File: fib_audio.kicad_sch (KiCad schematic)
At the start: 58 parts, among them J701 DNP AUDIO-JACK-8P-SMD, J702 SPK_JST_L, J703 SPK_JST_R, K701 BUTTON-4PDTSM-62K-S-V-T/R(SN4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, U701 WM8960CGEFL, X701 24MHz 306020014

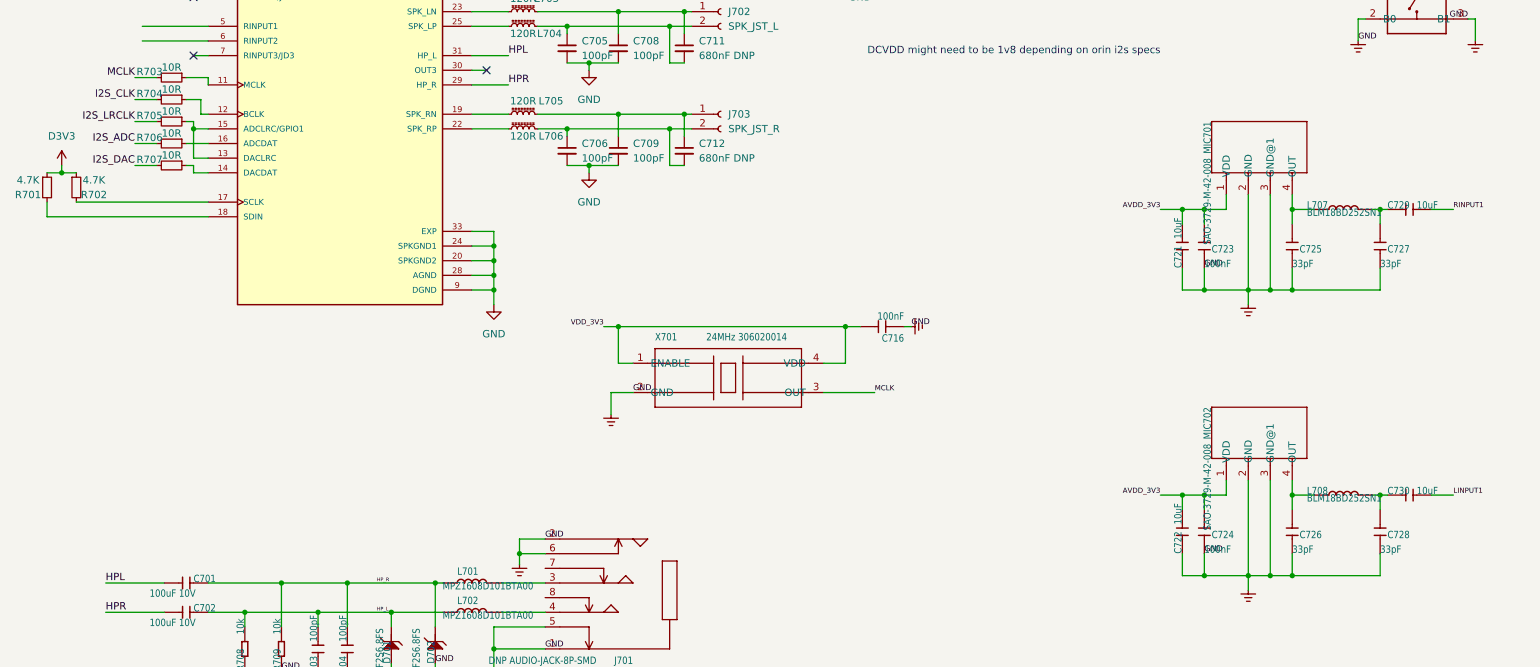
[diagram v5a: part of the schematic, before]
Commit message: added notest regarding the audio codec
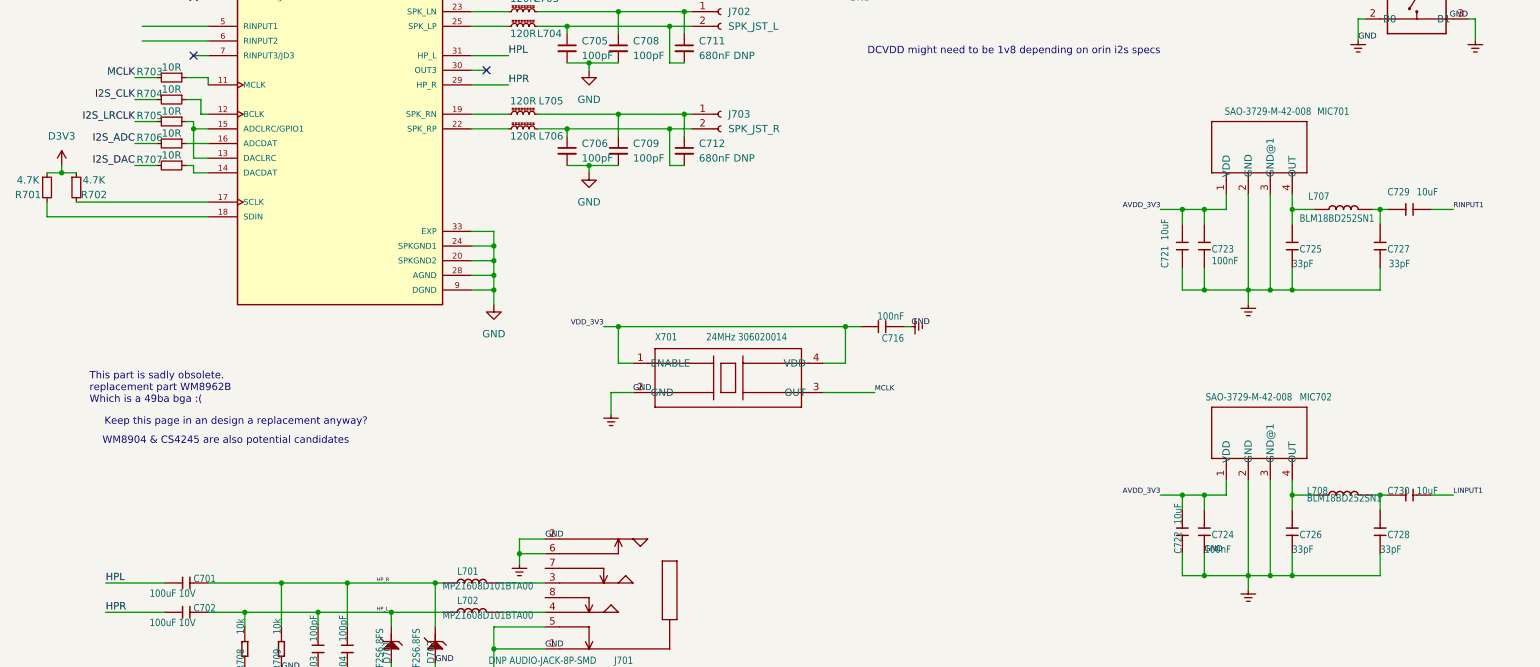
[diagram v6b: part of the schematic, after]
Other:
- note added: "Keep this page in an design a replacement anyway?"
- note added: "This part is sadly obsolete. replacement part WM8962B Which is a 49ba bga :("
- note added: "WM8904 & CS4245 are also potential candidates"
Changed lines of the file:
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@@
 	)
 	(junction
+		(at 222.25 95.25)
+		(diameter 0)
+		(color 0 0 0 0)
+	)
+	(junction
 		(at 140.97 36.83)
 		(diameter 0)
@@
 	)
 	(junction
-		(at 222.25 95.25)
-		(diameter 0)
-		(color 0 0 0 0)
-	)
-	(junction
 		(at 115.57 55.88)
 		(diameter 0)
@@
 	(wire
 		(pts
-			(xy 229.87 95.25) (xy 222.25 95.25)
-		)
-		(stroke
-			(width 0.1524)
-			(type solid)
-		)
-	)
-	(wire
-		(pts
 			(xy 132.08 46.99) (xy 133.35 46.99)
 		)
@@
 	(wire
 		(pts
+			(xy 222.25 95.25) (xy 229.87 95.25)
+		)
+		(stroke
+			(width 0)
+			(type default)
+		)
+	)
+	(wire
+		(pts
 			(xy 119.38 113.03) (xy 119.38 116.84)
 		)
@@
 	(wire
 		(pts
+			(xy 222.25 95.25) (xy 222.25 91.44)
+		)
+		(stroke
+			(width 0)
+			(type default)
+		)
+	)
+	(wire
+		(pts
 			(xy 130.81 31.75) (xy 130.81 36.83)
 		)
@@
 	(wire
 		(pts
-			(xy 222.25 91.44) (xy 222.25 95.25)
-		)
-		(stroke
-			(width 0.1524)
-			(type solid)
-		)
-	)
-	(wire
-		(pts
 			(xy 36.83 69.85) (xy 40.64 69.85)
 		)
@@
 		)
 	)
+	(text "WM8904 & CS4245 are also potential candidates"
+		(exclude_from_sim no)
+		(at 52.578 121.412 0)
+		(effects
+			(font
+				(size 1.27 1.27)
+			)
+		)
+	)
+	(text "This part is sadly obsolete.\nreplacement part WM8962B\nWhich is a 49ba bga :("
+		(exclude_from_sim no)
+		(at 28.956 112.268 0)
+		(effects
+			(font
+				(size 1.27 1.27)
+			)
+			(justify left)
+		)
+	)
+	(text "Keep this page in an design a replacement anyway?"
+		(exclude_from_sim no)
+		(at 54.356 118.11 0)
+		(effects
+			(font
+				(size 1.27 1.27)
+			)
+		)
+	)
 	(label "I2S_ADC"
 		(at 36.83 69.85 180)
@@
 	)
 	(label "GND"
-		(at 222.25 91.44 0)
-		(fields_autoplaced yes)
-		(effects
-			(font
-				(size 1.016 1.016)
-			)
-			(justify left bottom)
-		)
-	)
-	(label "GND"
 		(at 123.19 113.03 0)
 		(fields_autoplaced yes)
@@
 		(dnp no)
 		(property "Reference" "MIC702"
-			(at 223.52 115.57 0)
+			(at 244.348 114.554 90)
 			(effects
 				(font
@@
 		)
 		(property "Value" "SAO-3729-M-42-008"
-			(at 223.52 121.92 0)
+			(at 237.49 114.554 90)
 			(effects
 				(font
@@
 		(dnp no)
 		(property "Reference" "C729"
-			(at 254 81.28 0)
+			(at 254 78.994 0)
 			(effects
 				(font
@@
 		)
 		(property "Value" "10uF"
-			(at 259.08 81.28 0)
+			(at 259.08 78.994 0)
 			(effects
 				(font
@@
 		(dnp no)
 		(property "Reference" "MIC701"
-			(at 223.52 66.04 0)
+			(at 247.396 65.024 90)
 			(effects
 				(font
@@
 		)
 		(property "Value" "SAO-3729-M-42-008"
-			(at 223.52 72.39 0)
+			(at 240.792 65.024 90)
 			(effects
 				(font
@@
 		(dnp no)
 		(property "Reference" "L707"
-			(at 240.03 81.28 0)
+			(at 240.284 79.756 0)
 			(effects
 				(font
@@
 		)
 		(property "Value" "BLM18BD252SN1"
-			(at 240.03 82.55 0)
+			(at 238.76 83.566 0)
 			(effects
 				(font
@@
 		)
 		(property "Value" "33pF"
-			(at 252.73 91.44 90)
+			(at 254.254 91.44 90)
 			(effects
 				(font
@@
 		(dnp no)
 		(property "Reference" "C721"
-			(at 218.44 91.44 0)
+			(at 216.154 91.44 0)
 			(effects
 				(font
@@
 		)
 		(property "Value" "10uF"
-			(at 218.44 86.36 0)
+			(at 216.154 86.614 0)
 			(effects
 				(font
@@
 		)
 		(property "Value" "100nF"
-			(at 222.25 91.44 90)
+			(at 223.52 90.932 90)
 			(effects
 				(font

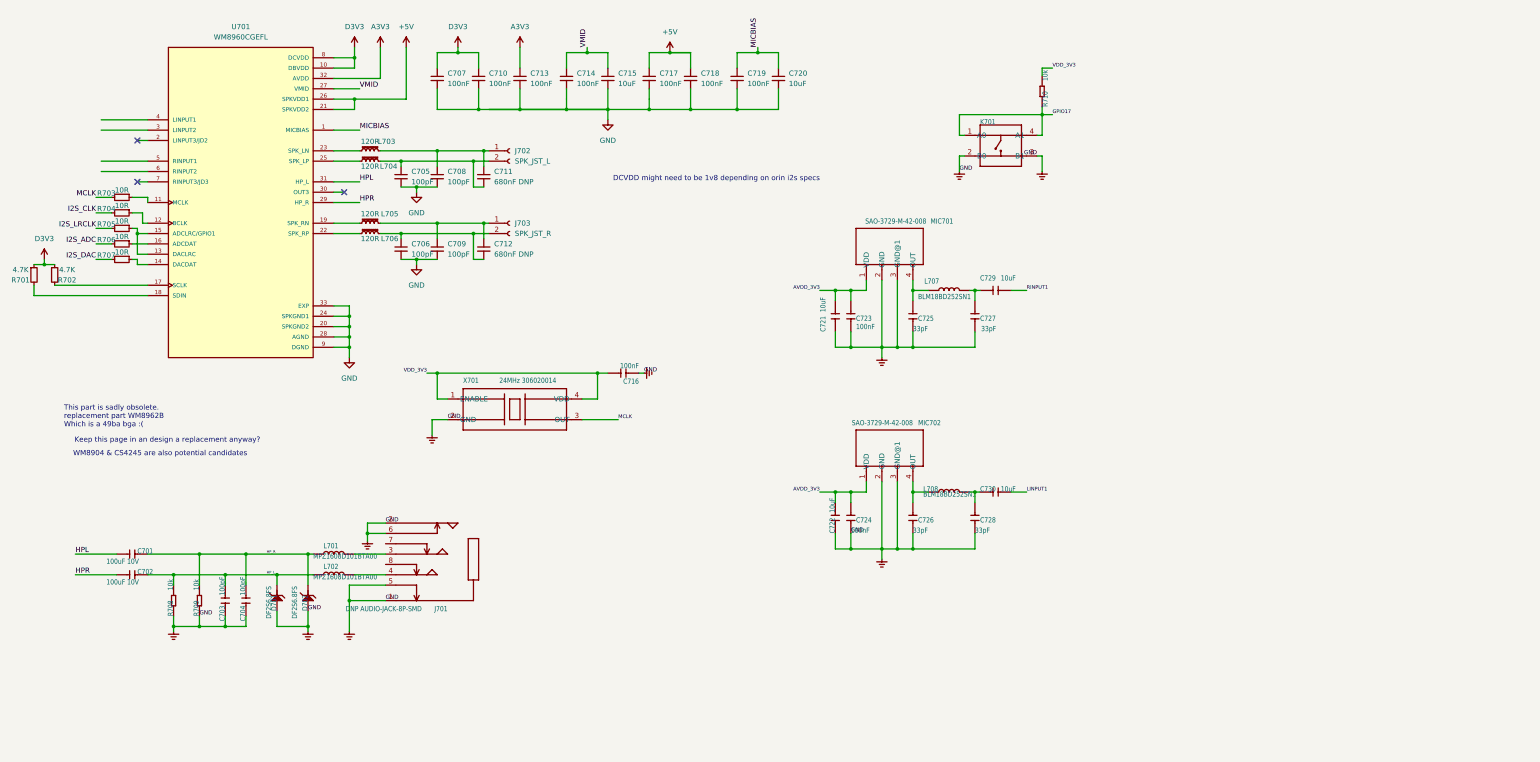
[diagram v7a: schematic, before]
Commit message: added some missing footprints, stared working ono power-on and sequencing
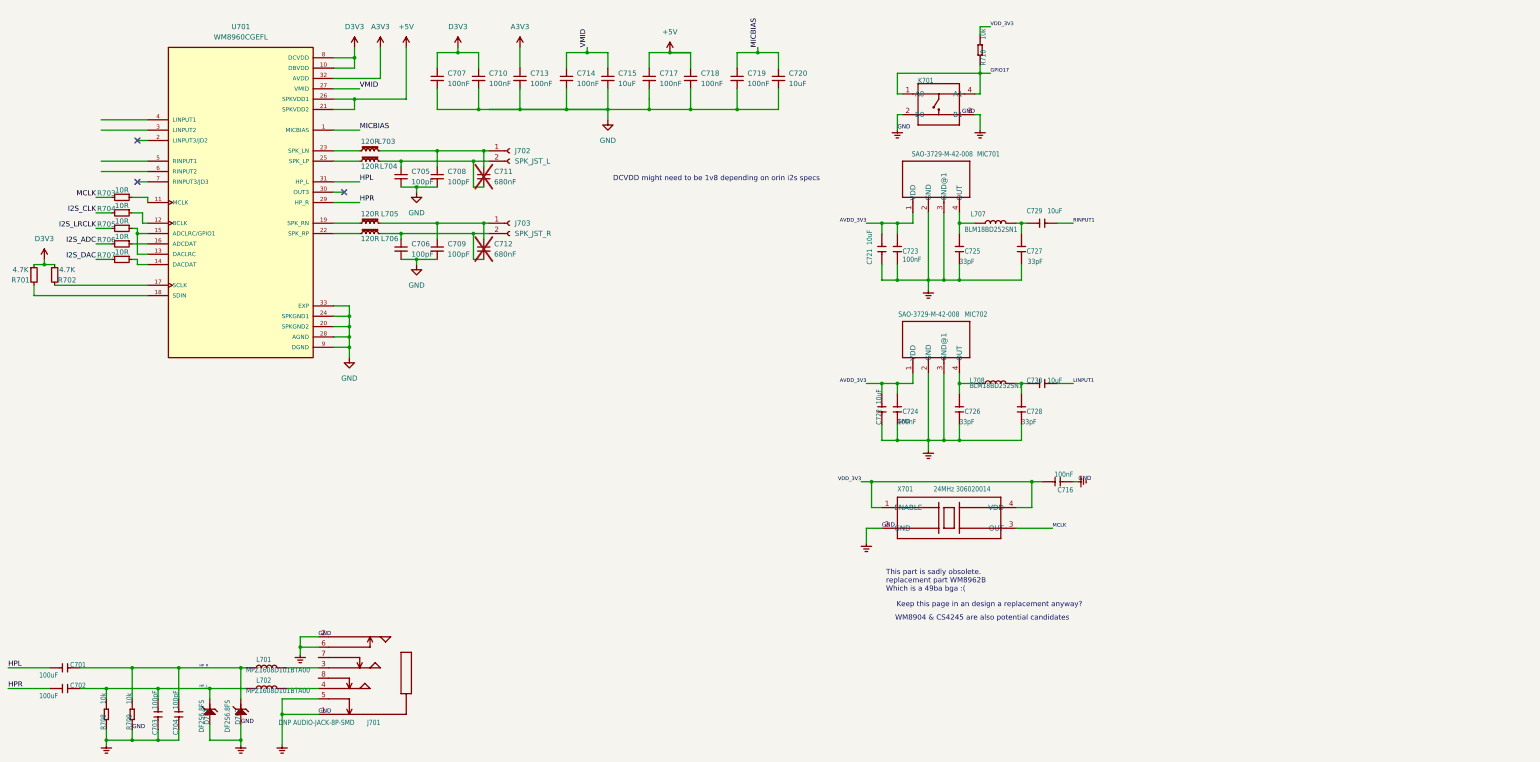
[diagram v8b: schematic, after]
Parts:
- C701, C702: value 100uF 10V -> 100uF
- C711, C712: value 680nF DNP -> 680nF; now not fitted
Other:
- moved on the sheet: C701, C702, C703, C704, C716, C721, C722, C723, C724, C725, C726, C727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
